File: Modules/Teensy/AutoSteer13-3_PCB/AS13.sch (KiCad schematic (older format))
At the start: 74 parts, among them IC1 AZ1117, IC2 XL2596, J1 U-USBAS04P-F000, J10 I2C-3V3, J11 I2C-3V3, J12 Conn_02x02_Counter_Clockwise, J13 Conn_01x15_Female, J14 Conn_01x08_Female, J15 BNO080_left, J16 BNO080_right, J17 Conn_01x15_Female, J18 Conn_01x08_Female, J19 Motor 2, J2 RS485, J20 Motor 1, J21 SF_F9P_left, J22 ArduSimple_tl, J23 ArduSimple_bl, J24 SF_F9P_right, J25 ArduSimple_tr, J26 ArduSimple_br, J27 Grove, J3 Teensy_USBhost, J4 HR911105A, J5 PM254V-11-06-H85, J6 DT13-12PA, J7 WemosD1_left, J8 Teensy_Ethernet, J9 WemosD1_right, K1 SRD-05VDC-SL-C, Q1 BC847, U1 SP3485EN-L/TR, U2 PC817X2CSP9F, U3 PC817X2CSP9F, U4 PC817X2CSP9F, U5 PC817X2CSP9F, U6 CC6900SO-10A

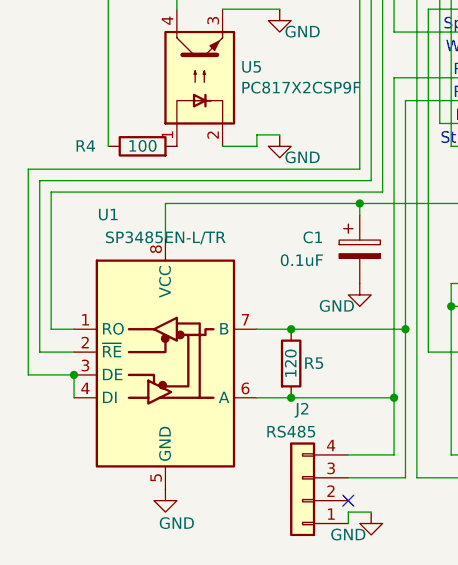
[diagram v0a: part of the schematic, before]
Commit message: fixed the RS485 circuit
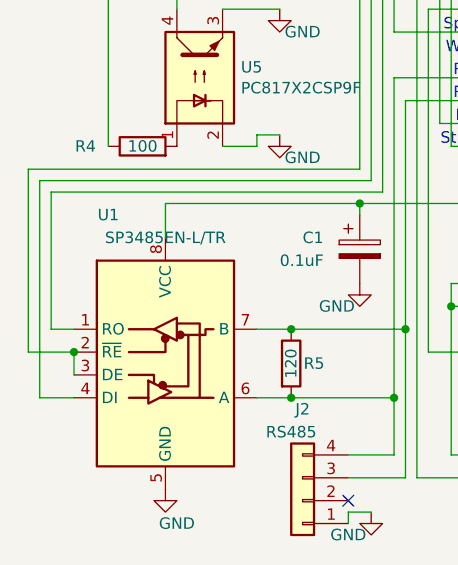
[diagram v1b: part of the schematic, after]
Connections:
- net at U1.2 (~RE): now also J14.3 (Pin_3), U1.3 (DE); no longer J14.5 (Pin_5)
- new net: J14.5 (Pin_5), U1.4 (DI)
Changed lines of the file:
@@
 encoding utf-8
 Sheet 1 1
-Title "AS13-2"
-Date "2022-03-13"
+Title "AS13-3"
+Date "2022-04-05"
 Rev ""
 Comp ""
@@
 Wire Wire Line
 	800  6850 700  6850
-Wire Wire Line
-	800  6950 650  6950
-Wire Wire Line
-	800  7050 800  7150
-Wire Wire Line
-	600  7050 800  7050
-Connection ~ 800  7050
 Text Notes 4200 3050 0    50   ~ 0
 5V
@@
 	700  6250 2150 6250
 Wire Wire Line
-	650  6950 650  6200
-Wire Wire Line
 	650  6200 2100 6200
 Wire Wire Line
-	600  7050 600  6150
-Wire Wire Line
 	600  6150 2050 6150
 Wire Wire Line
@@
 Text Notes 8600 5550 0    50   ~ 0
 5V
+Wire Wire Line
+	800  7150 650  7150
+Wire Wire Line
+	650  6200 650  7150
+Wire Wire Line
+	800  6950 600  6950
+Wire Wire Line
+	600  6950 600  6150
+Wire Wire Line
+	800  7050 800  6950
+Connection ~ 800  6950
 $EndSCHEMATC
